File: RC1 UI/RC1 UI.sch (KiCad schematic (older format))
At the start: 45 parts, among them J1 KB, J2 RC1_UI_Port, M1 Mounting, M2 Mounting, M3 Mounting, M4 Mounting, Q1 2N3906, Q2 2N3906, Q3 2N3906, Q4 2N3906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

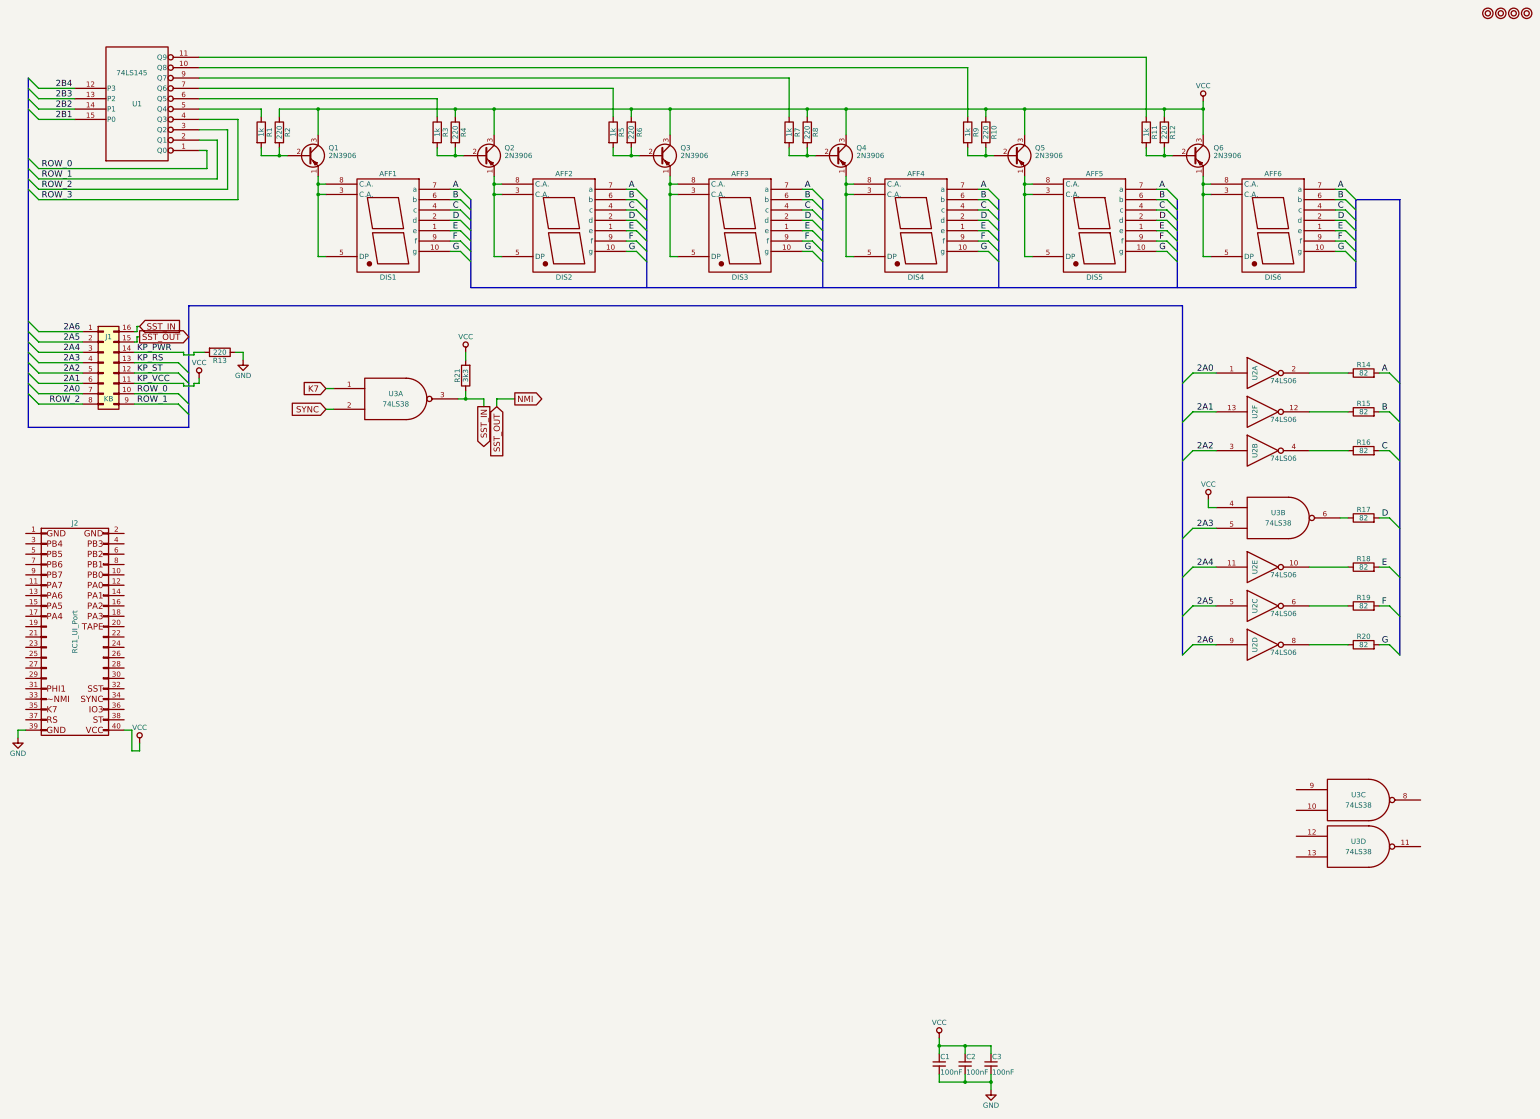
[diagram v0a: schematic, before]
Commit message: Added UI signals to CPU board
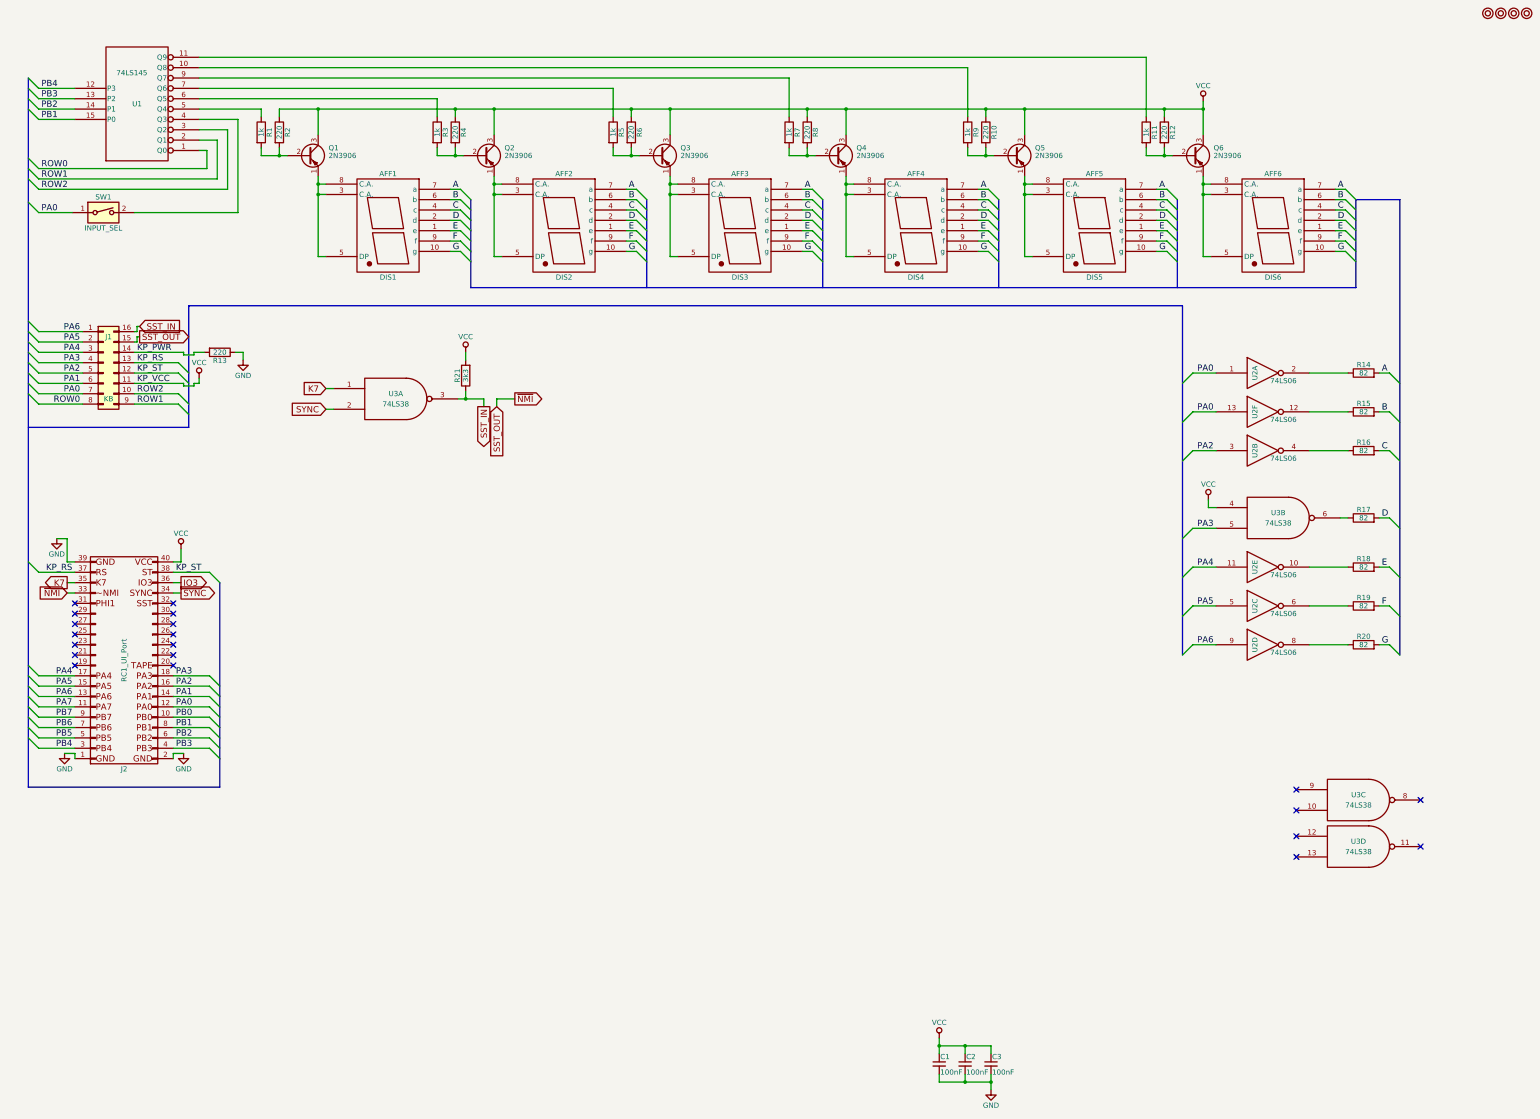
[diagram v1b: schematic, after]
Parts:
- added SW1: INPUT_SEL, symbol SW_DIP_x01
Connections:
- net 2A0 is gone; now on net PA0: J1.7 (Pin_7), U2.1
- net 2A2 is gone; now on net PA2: J1.5 (Pin_5), U2.3
- net 2A3 is gone; now on net PA3: J1.4 (Pin_4), U3.5
- net 2A4 is gone; now on net PA4: J1.3 (Pin_3), U2.11
- net 2A5 is gone; now on net PA5: J1.2 (Pin_2), U2.5
- net 2A6 is gone; now on net PA6: J1.1 (Pin_1), U2.9
- net 2B1 is gone; now on net PB1: U1.15 (P0)
- net 2B2 is gone; now on net PB2: U1.14 (P1)
- net 2B3 is gone; now on net PB3: U1.13 (P2)
- net 2B4 is gone; now on net PB4: U1.12 (P3)
- net NMI is gone; now on net SST_OUT: J1.15 (Pin_15)
- net GND: now also J2.1 (P1), J2.2 (P2)
- net K7: now also J2.35 (P35)
- net KP_RS: now also J2.37 (P37)
- net KP_ST: now also J2.38 (P38)
- net SYNC: now also J2.34 (P34)
- net PB0: now reaches J2.10 (P10)
- net PA7: now reaches J2.11 (P11)
- net PA0: now reaches J2.12 (P12)
- net PA0: now also U2.13, SW1.1
- net PA6: now reaches J2.13 (P13)
- net PA1: now reaches J2.14 (P14)
- net PA1: now also J1.6 (Pin_6)
- net PA5: now reaches J2.15 (P15)
- net PA2: now reaches J2.16 (P16)
- net PA4: now reaches J2.17 (P17)
- net PA3: now reaches J2.18 (P18)
- net PB4: now reaches J2.3 (P3)
- net SST_OUT: now reaches J2.33 (P33)
- net IO3: now reaches J2.36 (P36)
- net PB3: now reaches J2.4 (P4)
- net PB5: now reaches J2.5 (P5)
- net PB2: now reaches J2.6 (P6)
- net PB6: now reaches J2.7 (P7)
- net PB1: now reaches J2.8 (P8)
- net PB7: now reaches J2.9 (P9)
- removed net 2A1: J1.6 (Pin_6), U2.13
- net ROW_0 renamed ROW0
- net ROW0: now also J1.8 (Pin_8); no longer J1.10 (Pin_10)
- net ROW_1 renamed ROW1
- net ROW_2 renamed ROW2
- net ROW2: now also J1.10 (Pin_10); no longer J1.8 (Pin_8)
- net ROW_3: no longer names the net of U1.4 (Q3)
- net ROW_3: now also SW1.2
- no-connect marks 0 -> 20
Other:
- moved on the sheet: J2

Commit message: Added serial to UI schematic
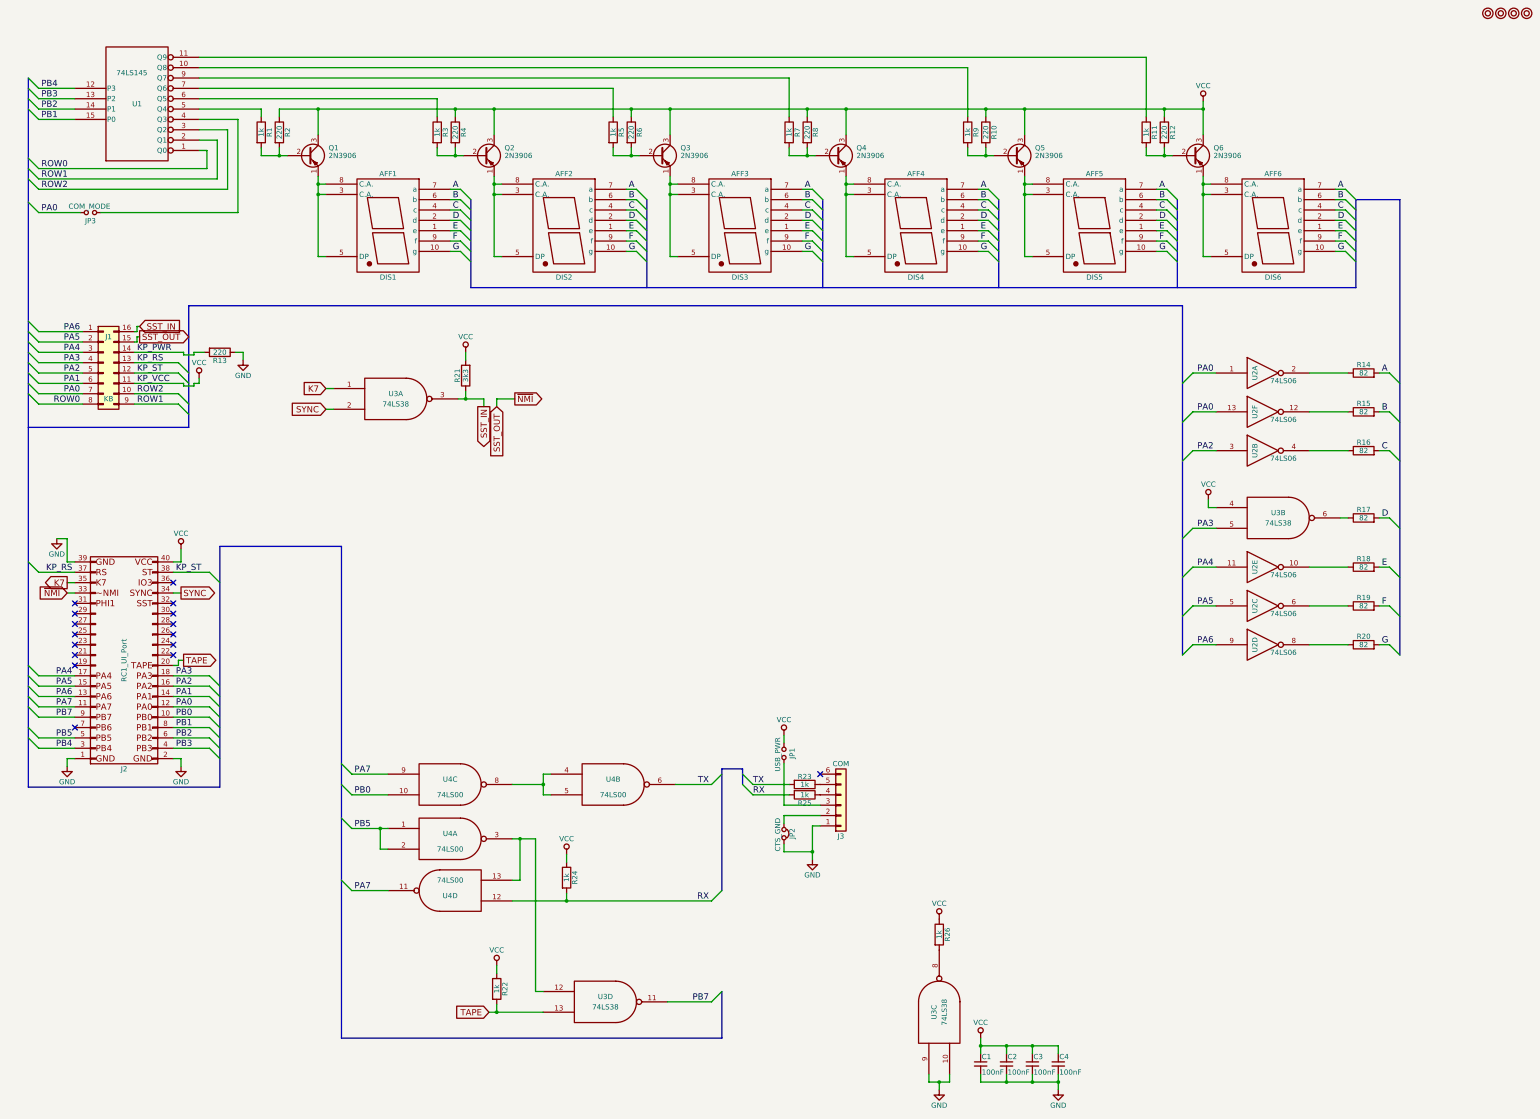
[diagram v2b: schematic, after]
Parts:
- removed SW1: INPUT_SEL, symbol SW_DIP_x01
- added C4: 100nF, Capacitors_THT:C_Disc_D4.7mm_W2.5mm_P5.00mm, symbol C_Small
- added J3: COM, Pin_Headers:Pin_Header_Angled_1x06_Pitch2.54mm, symbol Conn_01x06
- added JP1: USB_PWR, Pin_Headers:Pin_Header_Straight_1x02_Pitch2.54mm, symbol Jumper_NO_Small
- added JP2: CTS_GND, Pin_Headers:Pin_Header_Straight_1x02_Pitch2.54mm, symbol Jumper_NC_Small
- added JP3: COM_MODE, Pin_Headers:Pin_Header_Straight_1x02_Pitch2.54mm, symbol Jumper_NO_Small
- added R22, R23, R24, R25, R26: 1k, Resistors_THT:R_Axial_DIN0207_L6.3mm_D2.5mm_P5.08mm_Vertical, symbol R
- added U4: 74LS00, Housings_DIP:DIP-14_W7.62mm_Socket, symbol 74LS00
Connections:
- net GND: now also U3.10, U3.9, C4.2, J3.1 (Pin_1), JP2.2, U4.7 (GND), U4.7 (GND), U4.7 (GND), U4.7 (GND)
- net PA0: now also JP3.2
- net PA7: now also U4.11, U4.9
- net PB0: now also U4.10
- net PB5: now also U4.1, U4.2
- net PB7: now also U3.11
- net VCC: now also C4.1, JP1.1, R22.1, R24.1, R26.1, U4.14 (VCC), U4.14 (VCC), U4.14 (VCC), U4.14 (VCC)
- net at U1.4 (Q3): now also JP3.1
- net at U3.8: now also R26.2
- net at U3.12: now also U4.13, U4.3
- net TAPE: now reaches U3.13
- net TAPE: now also J2.20 (P20), R22.2
- net IO3: no longer names the net of J2.36 (P36)
- net PB6: no longer names the net of J2.7 (P7)
- new net: U4.4, U4.5, U4.8
- new net: J3.2 (Pin_2), JP2.1
- new net: J3.3 (Pin_3), JP1.2
- new net: J3.4 (Pin_4), R25.1
- new net: J3.5 (Pin_5), R23.1
- new net RX: R24.2, R25.2, U4.12
- new net TX: R23.2, U4.6
- no-connect marks 20 -> 16
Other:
- moved on the sheet: C1, C2, C3, U3C, U3D

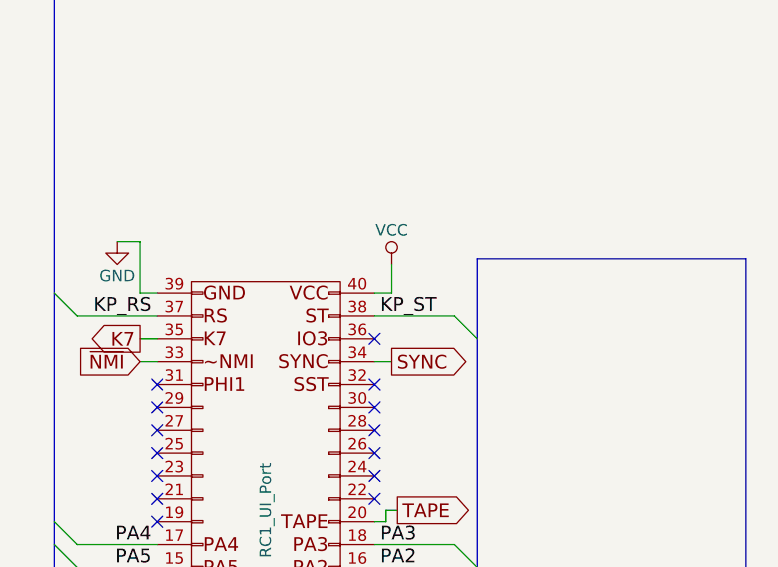
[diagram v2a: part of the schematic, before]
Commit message: Added phi1 to UI connector
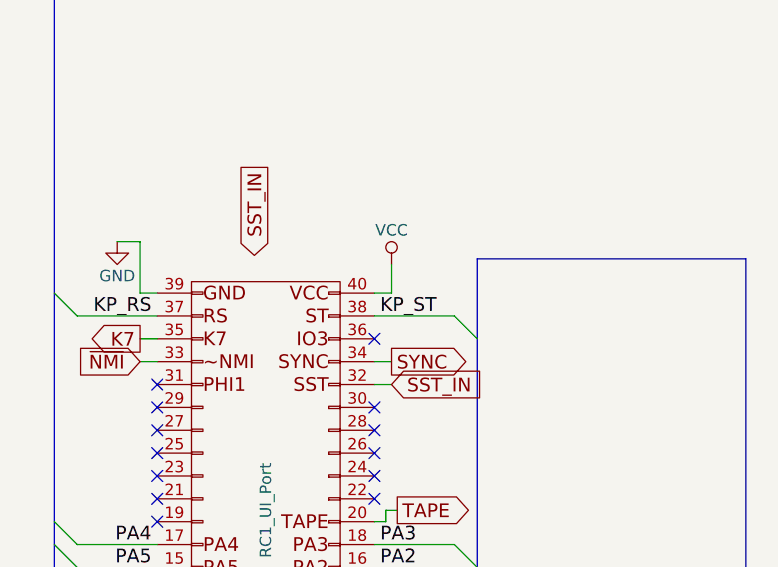
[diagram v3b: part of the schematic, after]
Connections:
- net SST_IN: now also J2.32 (P32)
- no-connect marks 16 -> 15
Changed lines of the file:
@@
 Text Label 1950 7250 2    60   ~ 0
 PA7
-NoConn ~ 2925 6250
 NoConn ~ 2925 6350
 NoConn ~ 2925 6450
@@
 	-1   0    0    1
 $EndComp
+Text GLabel 2400 5300 3    60   Output ~ 0
+SST_IN
+Text GLabel 3000 6250 2    60   Input ~ 0
+SST_IN
+Wire Wire Line
+	2925 6250 3000 6250
 $EndSCHEMATC
